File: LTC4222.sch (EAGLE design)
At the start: 25 parts, among them J1 67997-100HLF, Q1 PMV15ENEAR, Q2 PMV15ENEAR

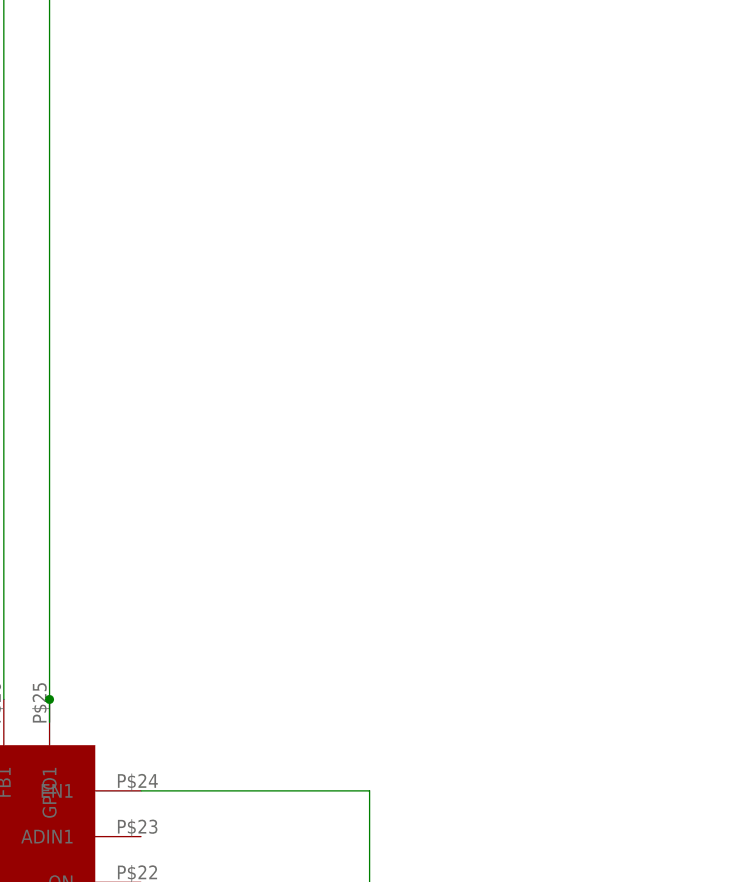
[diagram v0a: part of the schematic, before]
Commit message: Add LTC4222
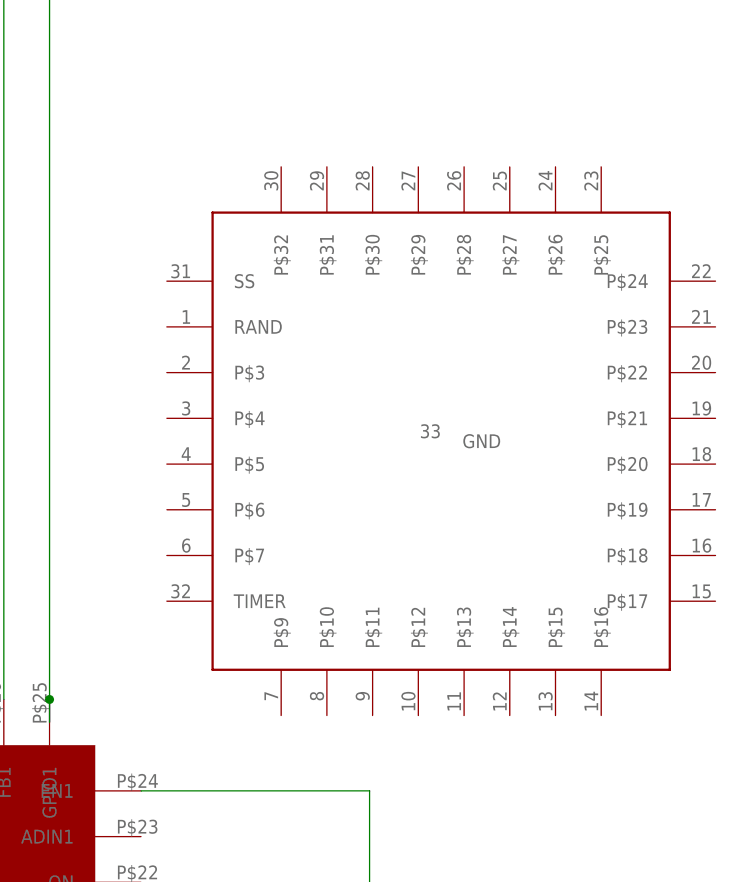
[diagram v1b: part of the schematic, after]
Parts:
- added U$12: LTC4222, Baja_Parts_Lib:LTC4222
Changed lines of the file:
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@@
 <part name="C5" library="SamacSys_Parts" deviceset="CGA2B3X7R1E683K050BB" device=""/>
 <part name="X_6" library="ngspice-simulation" library_urn="urn:adsk.eagle:library:527439" deviceset="GND" device=""/>
+<part name="U$12" library="Baja_Parts_Lib" deviceset="LTC4222" device="" package3d_urn="urn:adsk.eagle:package:31665535/1"/>
 </parts>
 <sheets>
@@
 </instance>
 <instance part="X_6" gate="G$1" x="5.08" y="45.72" smashed="yes"/>
+<instance part="U$12" gate="G$1" x="99.39589375" y="97.2754875" smashed="yes"/>
 </instances>
 <busses>
@@
 will not be understood (or retained) with this version.
 </note>
+<note version="8.3" severity="warning">
+Since Version 8.3, EAGLE supports the association of 3D packages
+with devices in libraries, schematics, and board files. Those 3D
+packages will not be understood (or retained) with this version.
+</note>
 </compatibility>

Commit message: LTC4222 Version 1.0 w/o flip flop
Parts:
- removed C1, C3: CGA3E2X7R1H104K080AE, SamacSys_Parts:CGA3E2X7R1H104K080AE
- removed C2: CGA2B3X7R1V223K050BB, SamacSys_Parts:CGA2B3X7R1V223K050BB
- removed C4: CGA3E1X7R1V105K080AE, SamacSys_Parts:CGA3E1X7R1V105K080AE
- removed C5: CGA2B3X7R1E683K050BB, SamacSys_Parts:CGA2B3X7R1E683K050BB
- removed J1: 67997-100HLF, SamacSys_Parts:67997-100HLF
- removed Q1, Q2: PMV15ENEAR, SamacSys_Parts:PMV15ENEAR
- removed R1, R5: TNPW060310R0BEEN, SamacSys_Parts:TNPW060310R0BEEN
- removed R2: MCT0603PD4991DP500, SamacSys_Parts:MCT0603PD4991DP500
- removed R3, R6: TNPW060310K0BEEA, SamacSys_Parts:TNPW060310K0BEEA
- removed R4: TNPW06031K02BEEA, SamacSys_Parts:TNPW06031K02BEEA
- removed U$1: DUMMY_LTC, SamacSys_Parts:DUMMY_LTC
- removed U$10: 10.2K_DUMMY, SamacSys_Parts:10.2K_DUMMY
- removed U$11, U$6: 3.57K_DUMMY, SamacSys_Parts:3.57K_DUMMY
- removed U$2: 1.8K_DUMMY, SamacSys_Parts:1.8K_DUMMY
- removed U$3: 392_DUMMY, SamacSys_Parts:392_DUMMY
- removed U$4: 953_DUMMY, SamacSys_Parts:953_DUMMY
- removed U$5, U$9: 18MILLI_DUMMY, SamacSys_Parts:18MILLI_DUMMY
- removed U$7: 34K_DUMMY, SamacSys_Parts:34K_DUMMY
- removed U$8: 3.4K_DUMMY, SamacSys_Parts:3.4K_DUMMY
- added U$13: AT0603DRD071K82L, Baja_Parts_Lib:AT0603DRD071K82L
- added U$14: TNPW0603392RBEEA, Baja_Parts_Lib:TNPW0603392RBEEA
- added U$15: TNPW0603953RBEEA, Baja_Parts_Lib:TNPW0603953RBEEA
- added U$16: CGA3E1X7R1V105K080AE, Baja_Parts_Lib:CGA3E1X7R1V105K080AE
- added U$17: CGA2B3X7R1E683K050BB, Baja_Parts_Lib:CGA2B3X7R1E683K050BB
- added U$18: CGA3E2X7R1H104K080AE, Baja_Parts_Lib:CGA3E2X7R1H104K080AE
- added U$19, U$30: WSL0603R0180FEA, Baja_Parts_Lib:WSL0603R0180FEA
- added U$20, U$31: PMV15ENEAR, Baja_Parts_Lib:PMV15ENEAR
- added U$21, U$32: TNPW060310R0BEEN, Baja_Parts_Lib:TNPW060310R0BEEN
- added U$22: 67997-100HLF, Baja_Parts_Lib:67997-100HLF
- added U$23: CGA2B3X7R1V223K050BB, Baja_Parts_Lib:CGA2B3X7R1V223K050BB
- added U$24, U$33: MCT0603PD4991DP500, Baja_Parts_Lib:MCT0603PD4991DP500
- added U$25, U$34: TNPW06033K57BEEA, Baja_Parts_Lib:TNPW06033K57BEEA
- added U$26, U$35: TNPW060310K0BEEA, Baja_Parts_Lib:TNPW060310K0BEEA
- added U$27: TNPW060334K0BEEA, Baja_Parts_Lib:TNPW060334K0BEEA
- added U$28: TNPW06031K02BEEA, Baja_Parts_Lib:TNPW06031K02BEEA
- added U$29: AT0603DRD073K4L, Baja_Parts_Lib:AT0603DRD073K4L
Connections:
- removed net 0: C1.2, C3.2, C4.1, C5.1, U$1.GND, U$11.2, U$4.2, U$6.2, U$8.2
- removed net N$1: C1.1, U$1.ADR2, U$1.CONFIG, U$1.INTVCC
- removed net N$10: R2.2, U$1.FB2, U$6.1
- removed net N$11: R3.2, U$1.GPIO2
- removed net N$12: C3.1, R4.1, U$1.OV1, U$7.2
- removed net N$13: R4.2, U$1.UV1, U$8.1
- removed net N$14: U$1.VDD1, U$7.1, U$9.1
- removed net N$15: Q2.D, U$1.SENSE1-, U$9.2
- removed net N$16: Q2.G, R5.1
- removed net N$17: R5.2, U$1.GATE1
- removed net N$18: Q2.S, R6.1, U$1.SOURCE1, U$10.1
- removed net N$19: U$1.FB1, U$10.2, U$11.1
- removed net N$2: U$1.OV2, U$3.2, U$4.1
- removed net N$20: U$1.EN1, U$1.EN2
- removed net N$21: R6.2, U$1.GPIO1
- removed net N$22: C4.2, U$1.TIMER
- removed net N$23: C5.2, U$1.SS
- removed net N$3: U$1.UV2, U$2.2, U$3.1
- removed net N$4: U$1.VDD2, U$2.1, U$5.1
- removed net N$5: Q1.D, U$1.SENSE2-, U$5.2
- removed net N$6: J1.1, Q1.G, R1.1
- removed net N$7: R1.2, U$1.GATE2
- removed net N$8: C2.2, J1.2
- removed net N$9: C2.1, Q1.S, R2.1, R3.1, U$1.SOURCE2
- new net GND: U$12.GND, U$15.P$2, U$16.1, U$17.1, U$18.1, U$25.P$2, U$29.P$2, U$34.P$2
- new net N$24: U$12.UV2, U$13.P$2, U$14.P$1
- new net N$25: U$12.OV2, U$14.P$2, U$15.P$1
- new net N$26: U$12.TIMER, U$16.2
- new net N$27: U$12.SS, U$17.2
- new net N$28: U$12.SENSE2-, U$19.P$1, U$20.D
- new net N$29: U$12.ADR2, U$12.CONFIG, U$12.INTVCC, U$18.2
- new net N$30: U$12.VDD2, U$13.P$1, U$19.P$2
- new net N$31: U$20.G, U$21.P$1, U$22.1
- new net N$32: U$12.GATE2, U$21.P$2
- new net N$33: U$22.2, U$23.2
- new net N$34: U$12.SOURCE2, U$20.S, U$23.1, U$24.P$1, U$26.P$1
- new net N$35: U$12.FB2, U$24.P$2, U$25.P$1
- new net N$36: U$12.OV1, U$28.P$2, U$29.P$1
- new net N$37: U$12.GPIO2, U$26.P$2
- new net N$38: U$12.UV1, U$27.P$2, U$28.P$1
- new net N$39: U$12.VDD1, U$27.P$1, U$30.P$1
- new net N$40: U$12.SENSE1-, U$30.P$2, U$31.S
- new net N$41: U$31.G, U$32.P$1
- new net N$42: U$12.GATE1, U$32.P$2
- new net N$43: U$12.SOURCE1, U$31.D, U$33.P$1, U$35.P$1
- new net N$44: U$12.GPIO1, U$35.P$2
- new net N$45: U$12.FB1, U$33.P$2, U$34.P$1

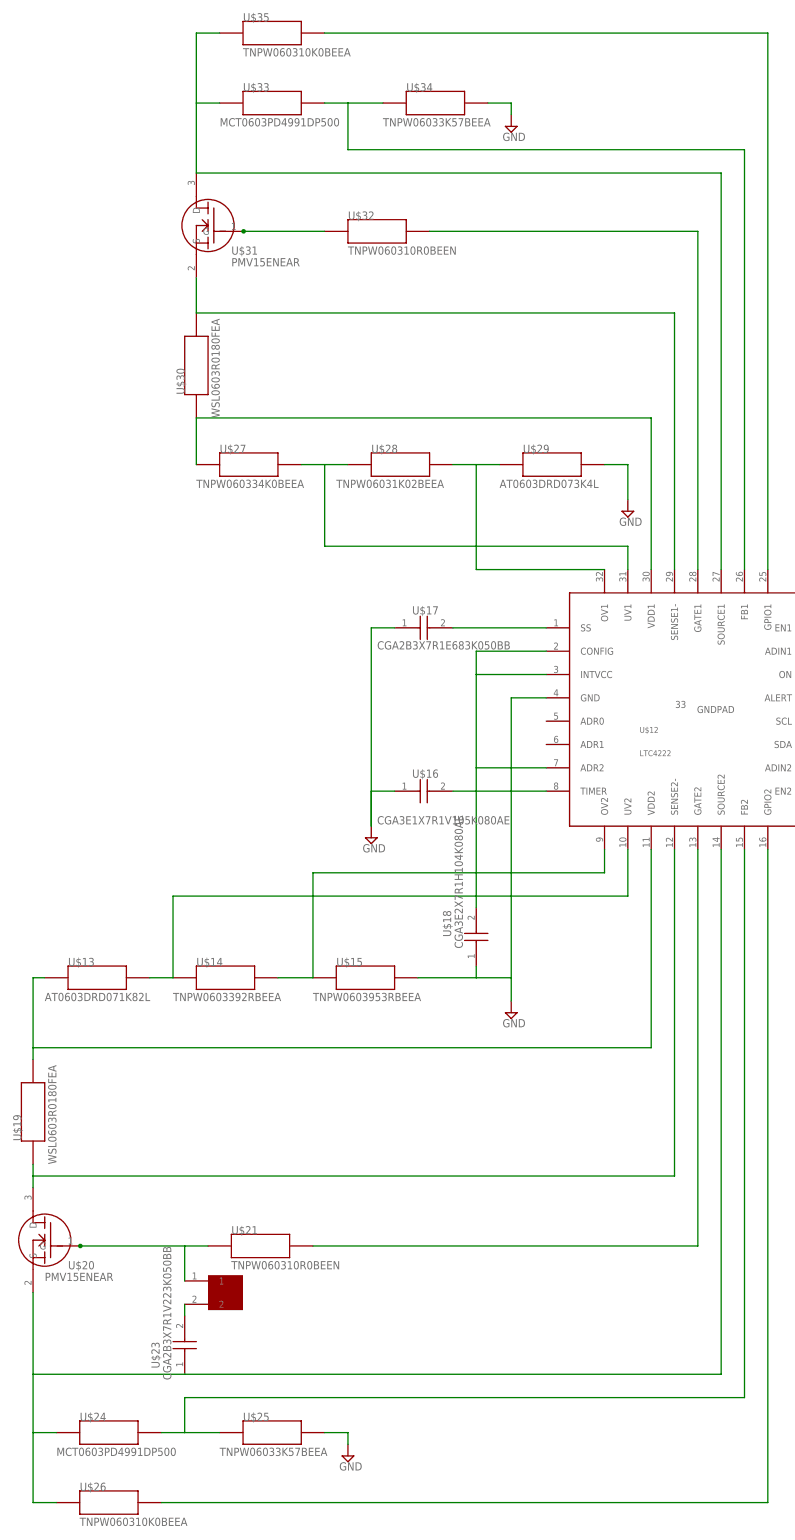
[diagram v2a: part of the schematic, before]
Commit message: Adjusted the LTC4222 to incorporate new 10k Ohm resistor after the first went out of stock
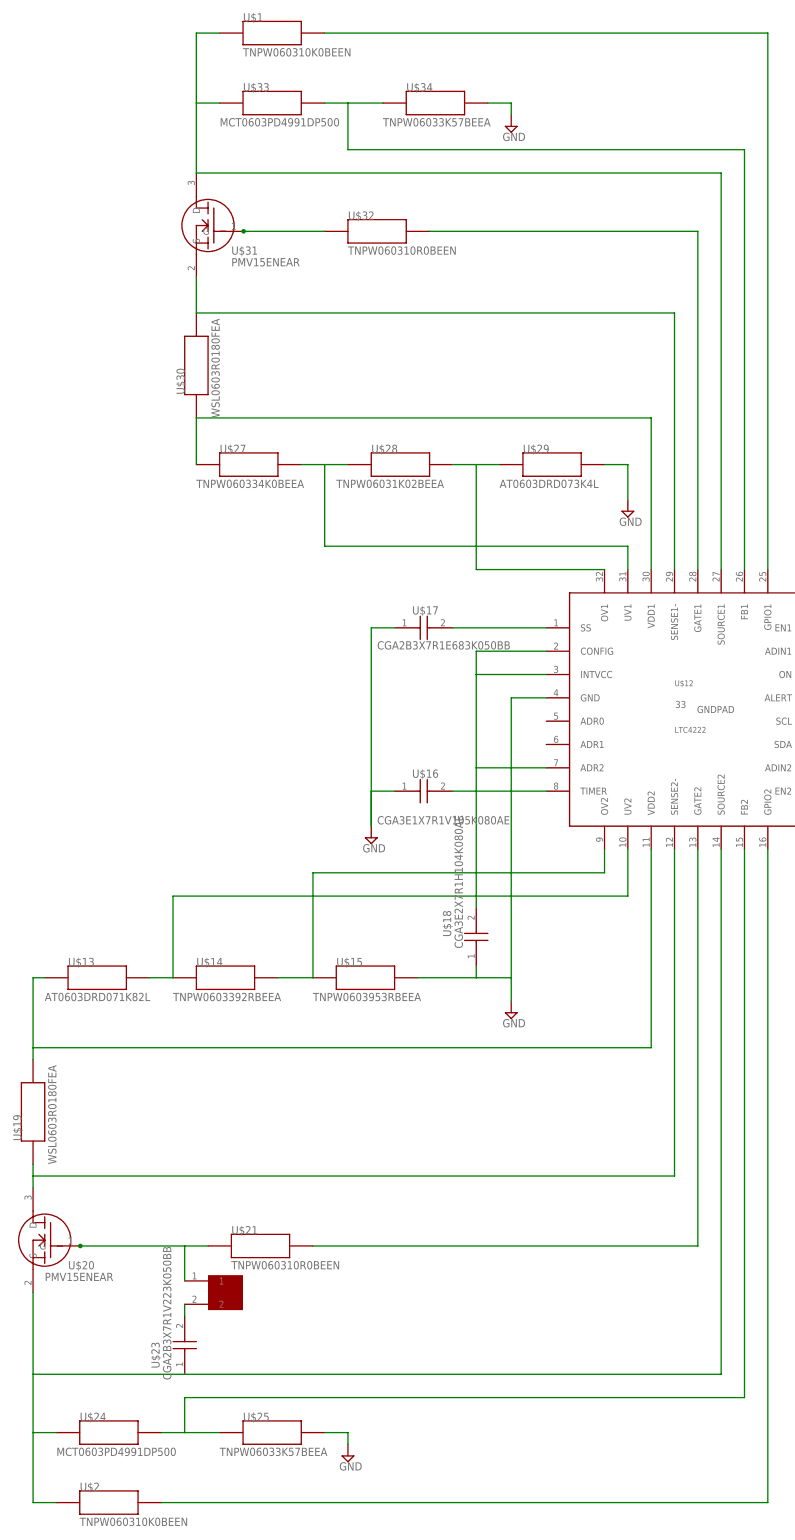
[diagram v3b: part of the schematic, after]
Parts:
- removed U$26, U$35: TNPW060310K0BEEA, Baja_Parts_Lib:TNPW060310K0BEEA
- added U$1, U$2: TNPW060310K0BEEN, Baja_Parts_Lib:TNPW060310K0BEEN
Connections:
- net N$34: now also U$2.P$1; no longer U$26.P$1
- net N$37: now also U$2.P$2; no longer U$26.P$2
- net N$43: now also U$1.P$1; no longer U$35.P$1
- net N$44: now also U$1.P$2; no longer U$35.P$2
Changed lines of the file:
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@@
 <part name="U$24" library="Baja_Parts_Lib" deviceset="MCT0603PD4991DP500" device="" package3d_urn="urn:adsk.eagle:package:31668671/1"/>
 <part name="U$25" library="Baja_Parts_Lib" deviceset="TNPW06033K57BEEA" device="" package3d_urn="urn:adsk.eagle:package:31668595/1"/>
-<part name="U$26" library="Baja_Parts_Lib" deviceset="TNPW060310K0BEEA" device="" package3d_urn="urn:adsk.eagle:package:31668595/1"/>
 <part name="SUPPLY3" library="supply2" library_urn="urn:adsk.eagle:library:372" deviceset="GND" device=""/>
 <part name="U$27" library="Baja_Parts_Lib" deviceset="TNPW060334K0BEEA" device="" package3d_urn="urn:adsk.eagle:package:31668595/1"/>
@@
 <part name="U$33" library="Baja_Parts_Lib" deviceset="MCT0603PD4991DP500" device="" package3d_urn="urn:adsk.eagle:package:31668671/1"/>
 <part name="U$34" library="Baja_Parts_Lib" deviceset="TNPW06033K57BEEA" device="" package3d_urn="urn:adsk.eagle:package:31668595/1"/>
-<part name="U$35" library="Baja_Parts_Lib" deviceset="TNPW060310K0BEEA" device="" package3d_urn="urn:adsk.eagle:package:31668595/1"/>
 <part name="SUPPLY5" library="supply2" library_urn="urn:adsk.eagle:library:372" deviceset="GND" device=""/>
+<part name="U$1" library="Baja_Parts_Lib" deviceset="TNPW060310K0BEEN" device="" package3d_urn="urn:adsk.eagle:package:31668595/1"/>
+<part name="U$2" library="Baja_Parts_Lib" deviceset="TNPW060310K0BEEN" device="" package3d_urn="urn:adsk.eagle:package:31668595/1"/>
 </parts>
 <sheets>
@@
 <instances>
 <instance part="U$12" gate="G$1" x="-147.32" y="38.1" smashed="yes">
-<attribute name="NAME" x="-132.08" y="58.42" size="1.27" layer="95"/>
-<attribute name="VALUE" x="-132.08" y="53.34" size="1.27" layer="96"/>
+<attribute name="NAME" x="-124.46" y="68.58" size="1.27" layer="95"/>
+<attribute name="VALUE" x="-124.46" y="58.42" size="1.27" layer="96"/>
 </instance>
 <instance part="U$13" gate="G$1" x="-261.62" y="5.08" smashed="yes">
@@
 <attribute name="VALUE" x="-223.52" y="-99.06" size="1.778" layer="96"/>
 </instance>
-<instance part="U$26" gate="G$1" x="-259.08" y="-109.22" smashed="yes">
-<attribute name="NAME" x="-254" y="-106.68" size="1.778" layer="95"/>
-<attribute name="VALUE" x="-254" y="-114.3" size="1.778" layer="96"/>
-</instance>
 <instance part="SUPPLY3" gate="GND" x="-195.58" y="-99.06" smashed="yes">
 <attribute name="VALUE" x="-197.485" y="-102.235" size="1.778" layer="96"/>
@@
 <attribute name="VALUE" x="-187.96" y="190.5" size="1.778" layer="96"/>
 </instance>
-<instance part="U$35" gate="G$1" x="-223.52" y="210.82" smashed="yes">
+<instance part="SUPPLY5" gate="GND" x="-160.02" y="190.5" smashed="yes">
+<attribute name="VALUE" x="-161.925" y="187.325" size="1.778" layer="96"/>
+</instance>
+<instance part="U$1" gate="G$1" x="-223.52" y="210.82" smashed="yes">
 <attribute name="NAME" x="-218.44" y="213.36" size="1.778" layer="95"/>
 <attribute name="VALUE" x="-218.44" y="205.74" size="1.778" layer="96"/>
 </instance>
-<instance part="SUPPLY5" gate="GND" x="-160.02" y="190.5" smashed="yes">
-<attribute name="VALUE" x="-161.925" y="187.325" size="1.778" layer="96"/>
+<instance part="U$2" gate="G$1" x="-259.08" y="-109.22" smashed="yes">
+<attribute name="NAME" x="-254" y="-106.68" size="1.778" layer="95"/>
+<attribute name="VALUE" x="-254" y="-114.3" size="1.778" layer="96"/>
 </instance>
 </instances>
@@
 <wire x1="-259.08" y1="-93.98" x2="-264.16" y2="-93.98" width="0.1524" layer="91"/>
 <wire x1="-264.16" y1="-93.98" x2="-264.16" y2="-81.28" width="0.1524" layer="91"/>
-<pinref part="U$26" gate="G$1" pin="P$1"/>
 <wire x1="-259.08" y1="-109.22" x2="-264.16" y2="-109.22" width="0.1524" layer="91"/>
 <wire x1="-264.16" y1="-109.22" x2="-264.16" y2="-93.98" width="0.1524" layer="91"/>
+<pinref part="U$2" gate="G$1" pin="P$1"/>
 </segment>
 </net>
@@
 <net name="N$37" class="0">
 <segment>
-<pinref part="U$26" gate="G$1" pin="P$2"/>
 <pinref part="U$12" gate="G$1" pin="GPIO2"/>
 <wire x1="-236.22" y1="-109.22" x2="-104.14" y2="-109.22" width="0.1524" layer="91"/>
 <wire x1="-104.14" y1="-109.22" x2="-104.14" y2="33.02" width="0.1524" layer="91"/>
+<pinref part="U$2" gate="G$1" pin="P$2"/>
 </segment>
 </net>
@@
 <pinref part="U$33" gate="G$1" pin="P$1"/>
 <wire x1="-223.52" y1="195.58" x2="-228.6" y2="195.58" width="0.1524" layer="91"/>
-<pinref part="U$35" gate="G$1" pin="P$1"/>
 <wire x1="-223.52" y1="210.82" x2="-228.6" y2="210.82" width="0.1524" layer="91"/>
 <wire x1="-228.6" y1="180.34" x2="-228.6" y2="195.58" width="0.1524" layer="91"/>
 <wire x1="-228.6" y1="210.82" x2="-228.6" y2="195.58" width="0.1524" layer="91"/>
+<pinref part="U$1" gate="G$1" pin="P$1"/>
 </segment>
 </net>
@@
 <net name="N$44" class="0">
 <segment>
-<pinref part="U$35" gate="G$1" pin="P$2"/>
 <pinref part="U$12" gate="G$1" pin="GPIO1"/>
 <wire x1="-200.66" y1="210.82" x2="-104.14" y2="210.82" width="0.1524" layer="91"/>
 <wire x1="-104.14" y1="210.82" x2="-104.14" y2="93.98" width="0.1524" layer="91"/>
-</segment>
-</net>
+<pinref part="U$1" gate="G$1" pin="P$2"/>
+</segment>
+</net>
